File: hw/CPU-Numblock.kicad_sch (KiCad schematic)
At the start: 32 parts, among them J2001 Conn_01x08, J2002 Conn_01x03, J2003 Conn_01x02, J2004 Conn_01x02, J2005 Conn_01x02, J2006 Conn_01x02, U2000 STM32F401XX-LQFP64, U2001 TLV62150A, Y2000 MCSJK-7I-8.00-18-30-60-B-30

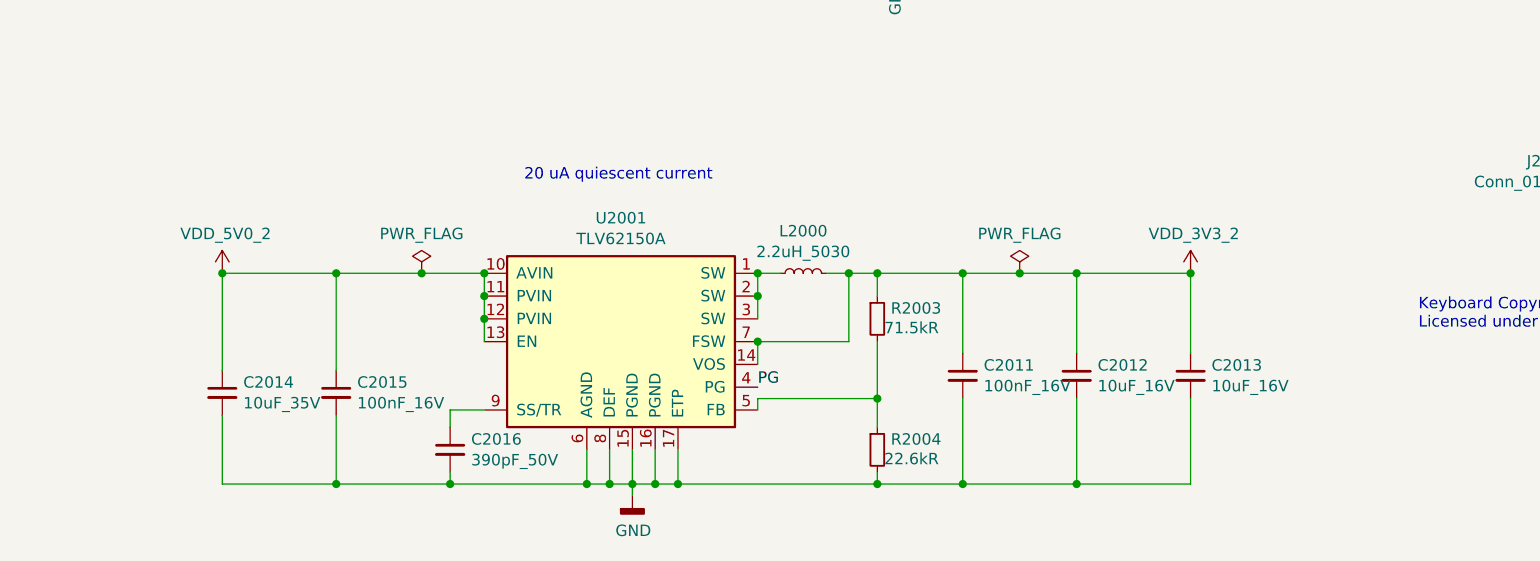
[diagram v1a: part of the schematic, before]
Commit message: Add current probes to 3.3V and pull-up to LV_EN.
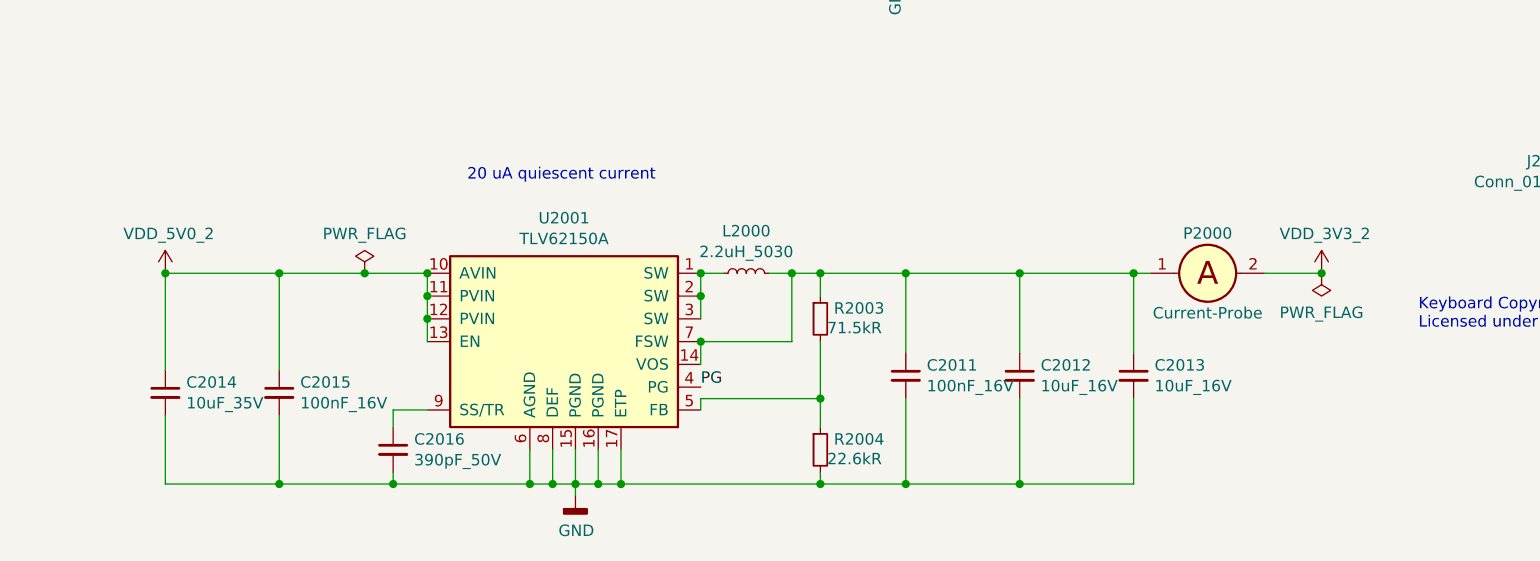
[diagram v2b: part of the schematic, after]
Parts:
- added P2000: Current-Probe, Keyboard:Current-Probe-2.54, symbol Keyboard:Current-Probe
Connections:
- net VDD_3V3_2: now also P2000.2; no longer C2011.1, C2012.1, C2013.1, L2000.2, R2003.1, U2001.14 (VOS), U2001.7 (FSW)
- new net: C2011.1, C2012.1, C2013.1, L2000.2, P2000.1, R2003.1, U2001.14 (VOS), U2001.7 (FSW)
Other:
- moved on the sheet: C2011, C2012, C2013, C2014, C2015, C2016, L2000, R2003, R2004, U2001
